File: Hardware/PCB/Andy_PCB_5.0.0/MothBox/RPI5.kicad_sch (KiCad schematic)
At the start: 37 parts, among them J5 Conn_01x05_Pin, SW1 SW_Push, U3 RASPBERRY_PI_5, U4 RASPBERRY_PI_4B_4GB, U5 STM32L031K6Tx, U6 TLV75733PDBVR, Y1 32.768kHz

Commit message: Andy Added Bolts an consolidated projects
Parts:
- U3, U4: now left out of the parts list
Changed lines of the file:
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@@
 		(unit 1)
 		(exclude_from_sim no)
-		(in_bom yes)
+		(in_bom no)
 		(on_board yes)
 		(dnp no)
@@
 		(unit 1)
 		(exclude_from_sim no)
-		(in_bom yes)
+		(in_bom no)
 		(on_board yes)
 		(dnp yes)

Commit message: made better camera
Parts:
- renumbered C16 to C10, C17 to C11, C7 to C12, C11 to C13, C10 to C14, C8 to C15, C9 to C6, C6 to C7, C14 to C8, C15 to C9, D33 to D1, D21 to D2, D22 to D3, D23 to D4, D24 to D5, D25 to D6, D26 to D7, D27 to D8, D28 to D9, J5 to J3, R9 to R10, R10 to R11, R11 to R6, R6 to R7, R7 to R8, R8 to R9, U3 to U5, U5 to U7

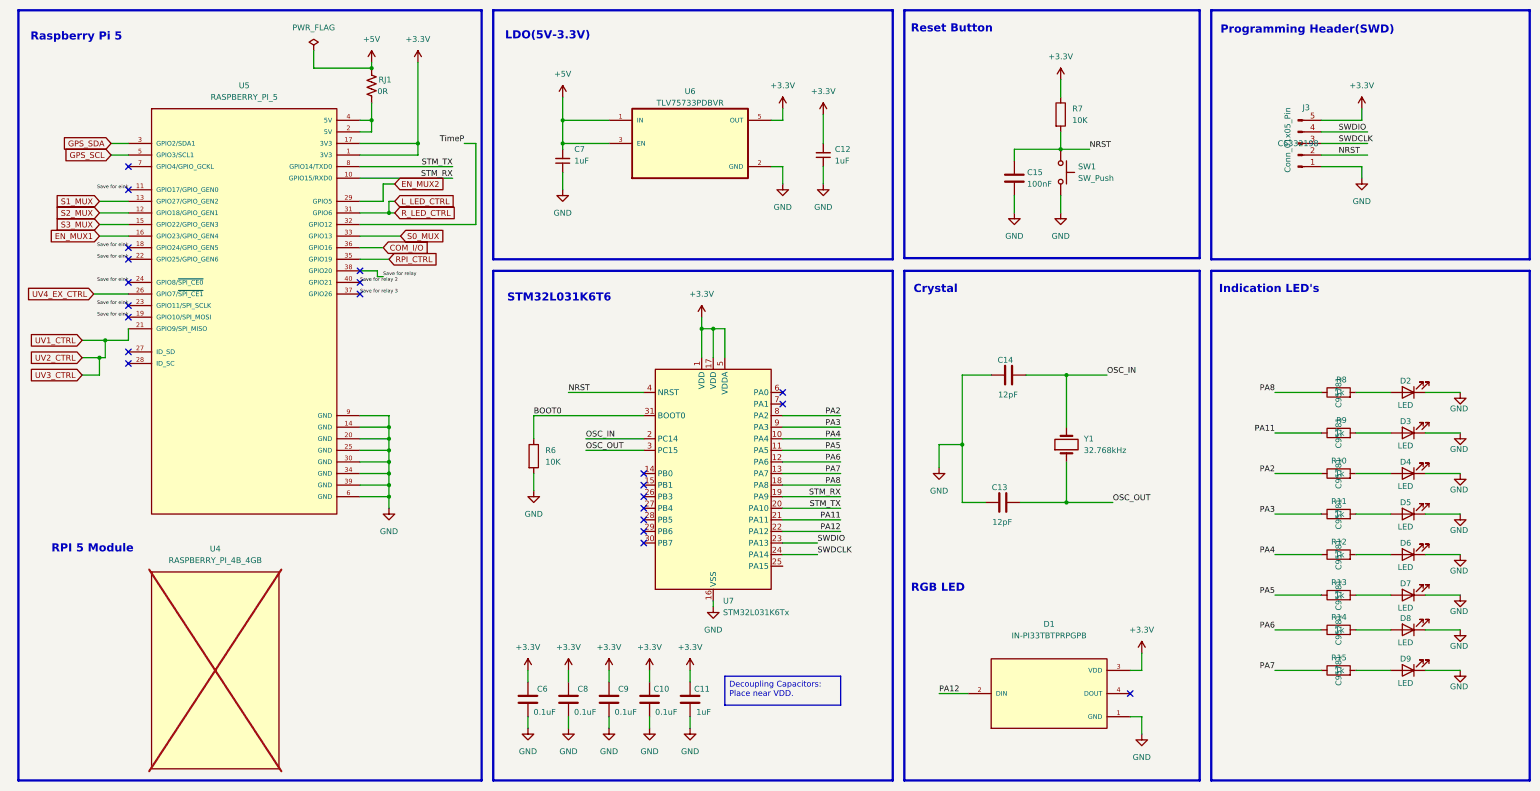
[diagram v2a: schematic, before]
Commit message: added female inverted header
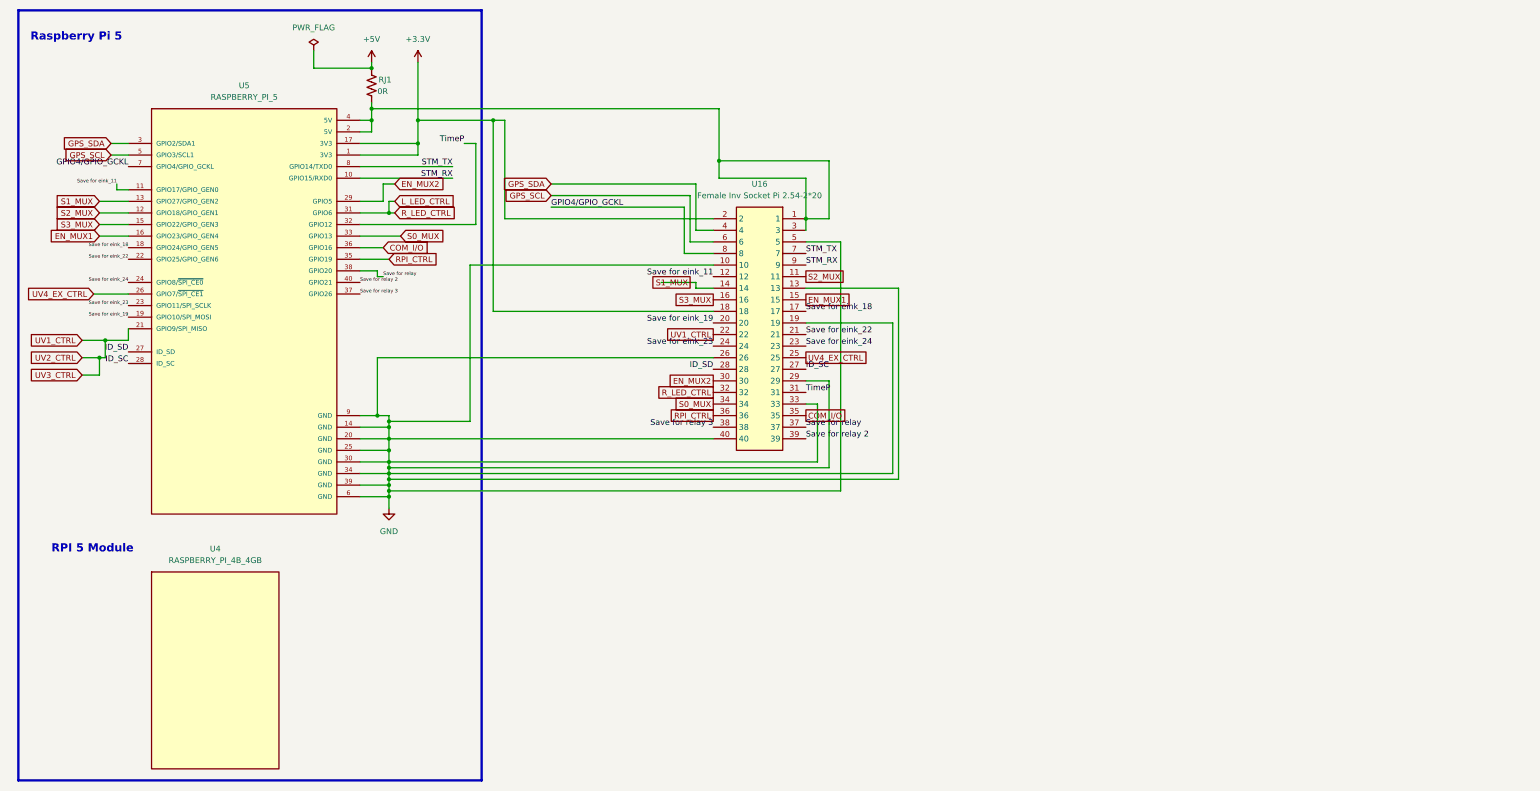
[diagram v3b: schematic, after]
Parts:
- removed C10, C6, C8, C9: 0.1uF, Capacitor_SMD:C_0805_2012Metric, symbol Device:C
- removed C11: 1uF, Capacitor_SMD:C_0805_2012Metric, symbol Device:C
- removed C12, C7: 1uF, Capacitor_SMD:C_0805_2012Metric, symbol Device:C_Small
- removed C13, C14: 12pF, Capacitor_SMD:C_0805_2012Metric, symbol Device:C
- removed C15: 100nF, Capacitor_SMD:C_0805_2012Metric, symbol Device:C
- removed D1: IN-PI33TBTPRPGPB, IN-PI33TBTPRPGPB:LED_IN-PI33TBTPRPGPB, symbol IN-PI33TBTPRPGPB:IN-PI33TBTPRPGPB
- removed D2, D3, D4, D5, D6, D7, D8, D9: LED, LED_SMD:LED_0805_2012Metric, symbol Device:LED
- removed J3: Conn_01x05_Pin, Connector_PinHeader_2.54mm:PinHeader_1x05_P2.54mm_Vertical, symbol Connector:Conn_01x05_Pin
- removed R10, R11, R12, R13, R14, R15, R8, R9: 1k, Resistor_SMD:R_0805_2012Metric, symbol Device:R
- removed R6, R7: 10K, Resistor_SMD:R_0805_2012Metric, symbol Device:R
- removed SW1: SW_Push, TS-1187A-B-A-B:SW_TS-1187A-B-A-B, symbol Switch:SW_Push
- removed U6: TLV75733PDBVR, TLV75733PDBVR:SOT95P280X145-5N, symbol TLV75733PDBVR:TLV75733PDBVR
- removed U7: STM32L031K6Tx, Package_QFP:LQFP-32_7x7mm_P0.8mm, symbol MCU_ST_STM32L0:STM32L031K6Tx
- removed Y1: 32.768kHz, Crystal:Crystal_SMD_3215-2Pin_3.2x1.5mm, symbol Device:Crystal
- added U16: Female Inv Socket Pi 2.54-2*20, easyeda2kicad:HDR-TH_40P-P2.54-V-F-R2-C20-S2.54, symbol easyeda2kicad:2.54-2*20
- U4: now fitted
- U5: now in the parts list
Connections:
- net +3.3V: now also U16.18, U16.2
- net COM_I/O: now also U16.35
- net EN_MUX1: now also U16.15
- net EN_MUX2: now also U16.30
- net GND: now also U16.10, U16.13, U16.19, U16.26, U16.29, U16.33, U16.40, U16.5
- net GPS_SCL: now also U16.6
- net GPS_SDA: now also U16.4
- net L_LED_CTRL: now also U16.32
- net RPI_CTRL: now also U16.36
- net S0_MUX: now also U16.34
- net S1_MUX: now also U16.14
- net S2_MUX: now also U16.11
- net S3_MUX: now also U16.16
- net STM_RX: now also U16.9
- net STM_TX: now also U16.7
- net Save for relay: now also U16.37
- net Save for relay 2: now also U16.39
- net Save for relay 3: now also U16.38
- net TimeP: now also U16.31
- net UV1_CTRL: now also U16.22
- net UV4_EX_CTRL: now also U16.25
- net at RJ1.2, U5.2 (5V), U5.4 (5V): now also U16.1, U16.3
- net ID_SD: now reaches U5.27 (ID_SD)
- net ID_SD: now also U16.28
- net ID_SC: now reaches U5.28 (ID_SC)
- net ID_SC: now also U16.27
- net GPIO4/GPIO_GCKL: now reaches U5.7 (GPIO4/GPIO_GCKL)
- net GPIO4/GPIO_GCKL: now also U16.8
- removed net Save for eink: U5.11 (GPIO17/GPIO_GEN0), U5.18 (GPIO24/GPIO_GEN5), U5.19 (GPIO10/SPI_MOSI), U5.22 (GPIO25/GPIO_GEN6), U5.23 (GPIO11/SPI_SCLK), U5.24 (GPIO8/~{SPI_CE0})
- new net Save for eink_11: U16.12, U5.11 (GPIO17/GPIO_GEN0)
- new net Save for eink_18: U16.17, U5.18 (GPIO24/GPIO_GEN5)
- new net Save for eink_19: U16.20, U5.19 (GPIO10/SPI_MOSI)
- new net Save for eink_22: U16.21, U5.22 (GPIO25/GPIO_GEN6)
- new net Save for eink_23: U16.24, U5.23 (GPIO11/SPI_SCLK)
- new net Save for eink_24: U16.23, U5.24 (GPIO8/~{SPI_CE0})
- no-connect marks 22 -> 0
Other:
- note removed: "Crystal"
- note removed: "Indication LED's"
- note removed: "LDO(5V-3.3V)"
- note removed: "Programming Header(SWD)"
- note removed: "RGB LED"
- note removed: "Reset Button"
- note removed: "STM32L031K6T6"

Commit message: made vertical pi
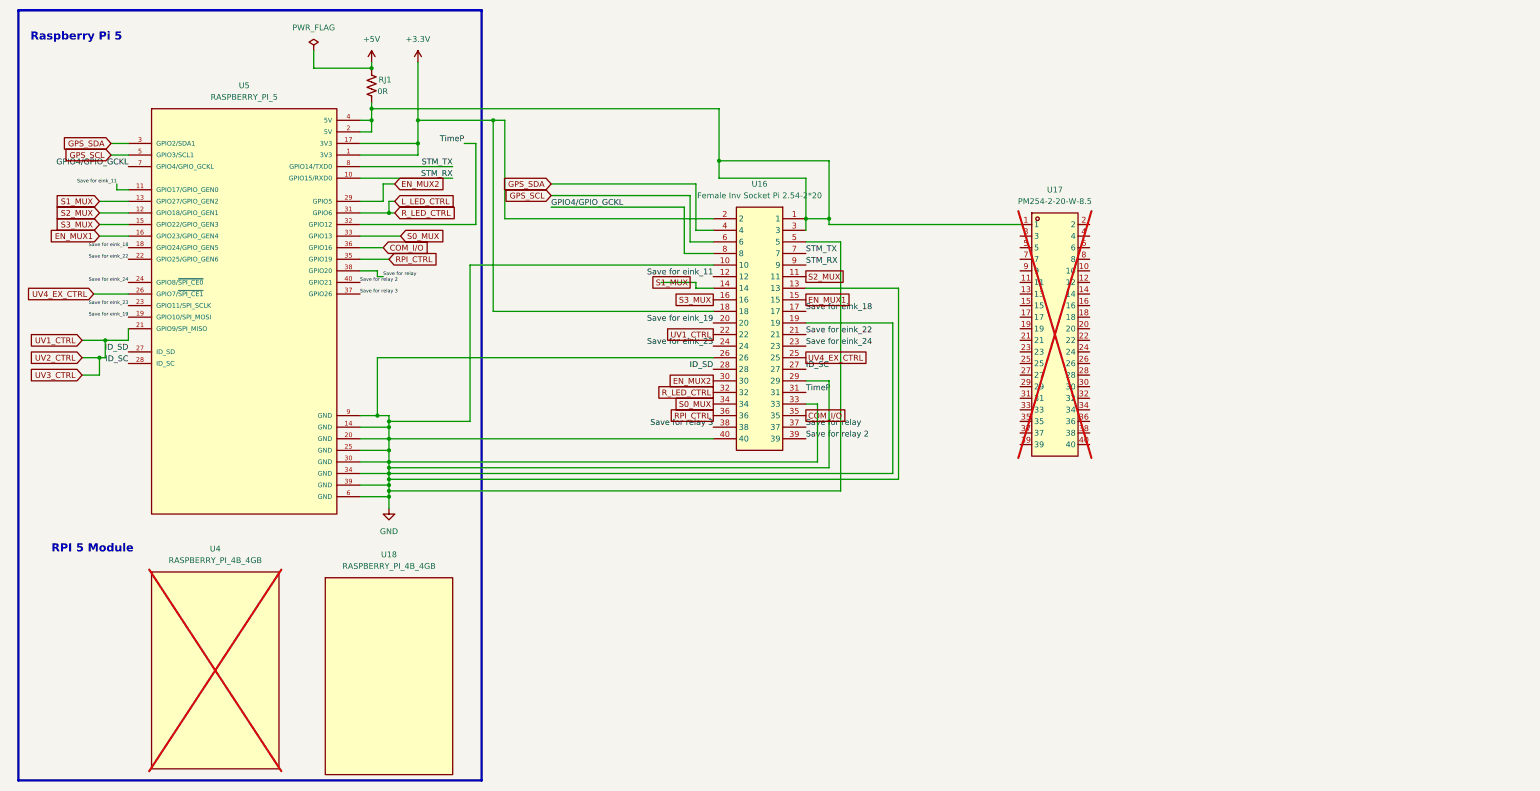
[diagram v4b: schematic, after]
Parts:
- added U17: PM254-2-20-W-8.5, easyeda2kicad:HDR-TH_40P-P2.54-H-F-R2-C20-W8.5, symbol easyeda2kicad:PM254-2-20-W-8.5
- added U18: RASPBERRY_PI_4B_4GB, RASPBERRY_PI_4B_4GB:MODULE_RASPBERRY_PI_4B_4GB_Sideways, symbol RASPBERRY_PI_4B_4GB:RASPBERRY_PI_4B_4GB
- U16: footprint easyeda2kicad:HDR-TH_40P-P2.54-V-F-R2-C20-S2.54 -> easyeda2kicad:HDR-TH_40P-P2.54-H-F-R2-C20-W8.5
- U4: now not fitted
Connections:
- net at RJ1.2, U16.1, U16.3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: now also U17.1

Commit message: arranged stuff better
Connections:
- net EN_MUX1 renamed EN_12VReg
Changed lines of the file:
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@@
+	(wire
+		(pts
+			(xy 195.58 80.01) (xy 194.31 80.01)
+		)
+		(stroke
+			(width 0)
+			(type default)
+		)
+	)
 	(wire
 		(pts
@@
 		)
 	)
-	(global_label "EN_MUX1"
+	(global_label "EN_12VReg"
 		(shape passive)
-		(at 194.31 80.01 0)
+		(at 195.58 80.01 0)
 		(effects
 			(font
@@
 		)
 		(property "Intersheetrefs" "${INTERSHEET_REFS}"
-			(at 194.31 80.01 0)
+			(at 195.58 80.01 0)
 			(effects
 				(font
@@
 		)
 	)
-	(global_label "EN_MUX1"
+	(global_label "EN_12VReg"
 		(shape input)
 		(at 39.37 66.04 180)

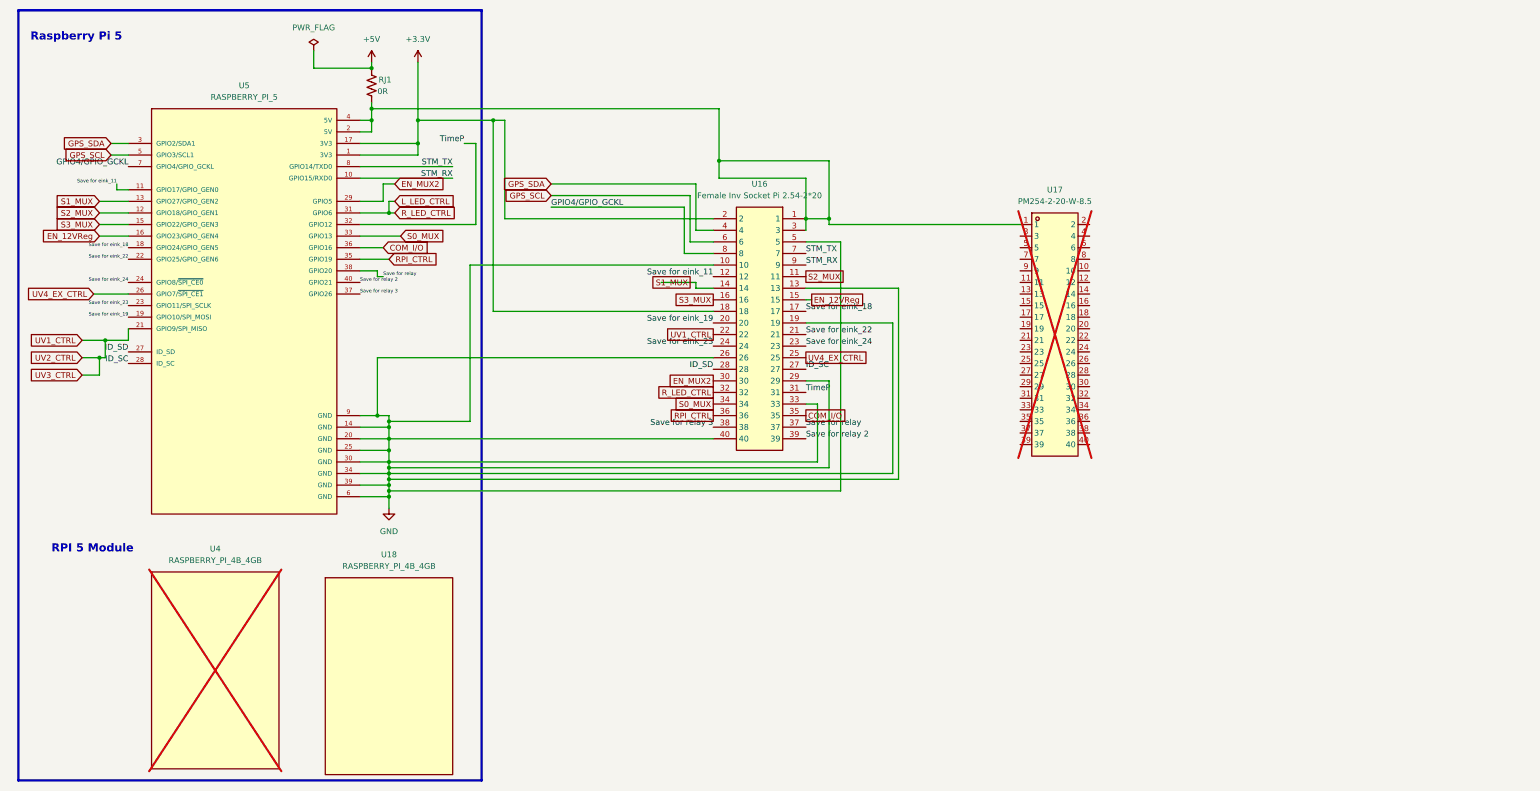
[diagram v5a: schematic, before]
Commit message: Added adafruit current sensor
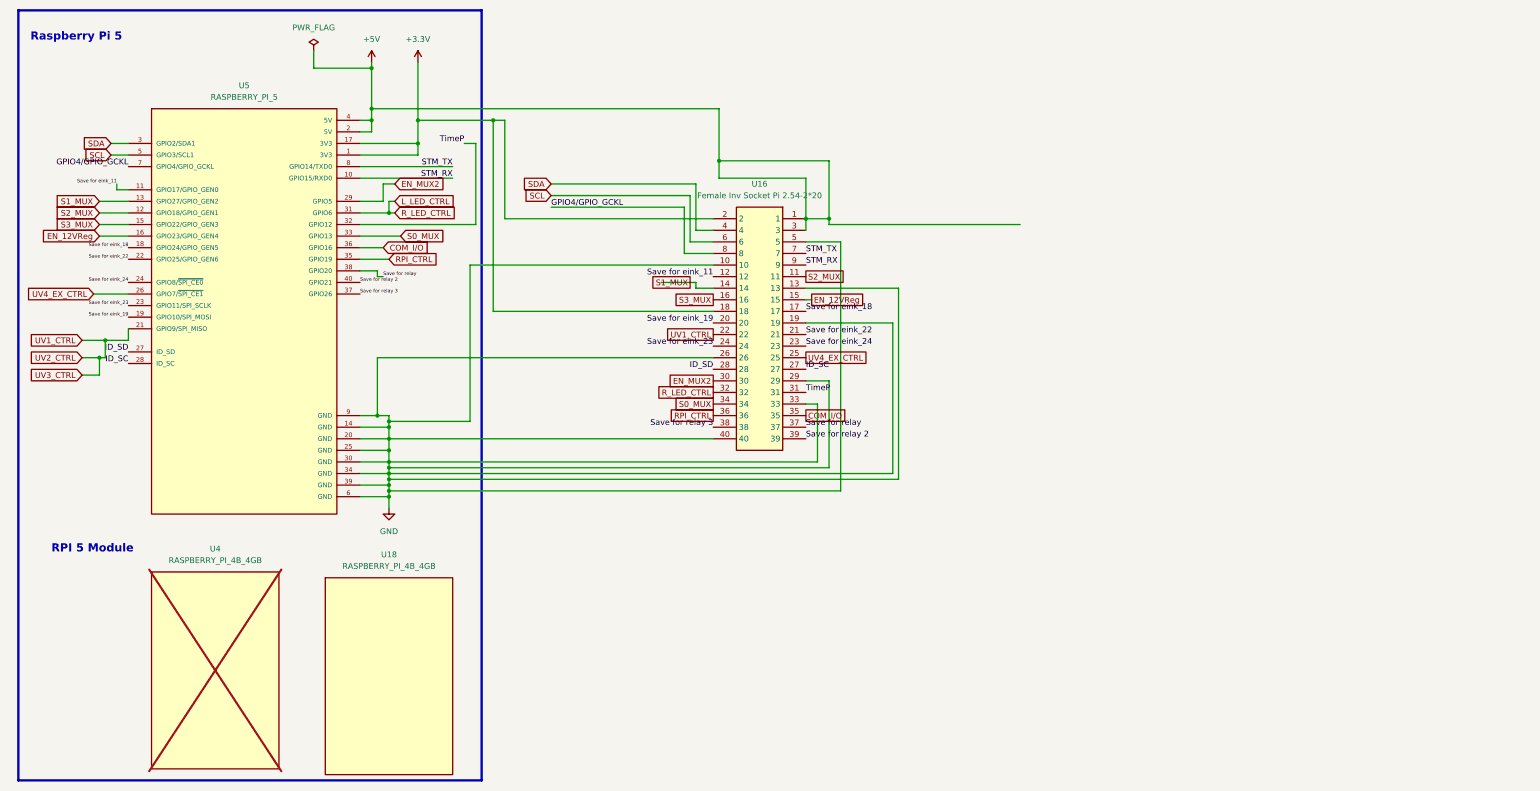
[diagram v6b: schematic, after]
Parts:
- removed RJ1: 0R, Resistor_SMD:R_2512_6332Metric, symbol Device:R_US
- removed U17: PM254-2-20-W-8.5, easyeda2kicad:HDR-TH_40P-P2.54-H-F-R2-C20-W8.5, symbol easyeda2kicad:PM254-2-20-W-8.5
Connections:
- net +5V: now also U16.1, U16.3, U5.2 (5V), U5.4 (5V)
- net GPS_SCL renamed SCL
- net GPS_SDA renamed SDA
